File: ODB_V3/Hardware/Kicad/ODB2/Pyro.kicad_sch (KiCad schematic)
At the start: 51 parts, among them J6 Screw_Terminal_01x08, Q2 MMBT3904, Q3 SI7617DN-T1-GE3, U10 SI5442DU-T1-GE3, U11 SI5442DU-T1-GE3, U12 SI5442DU-T1-GE3, U13 SI5442DU-T1-GE3, U6 LM339

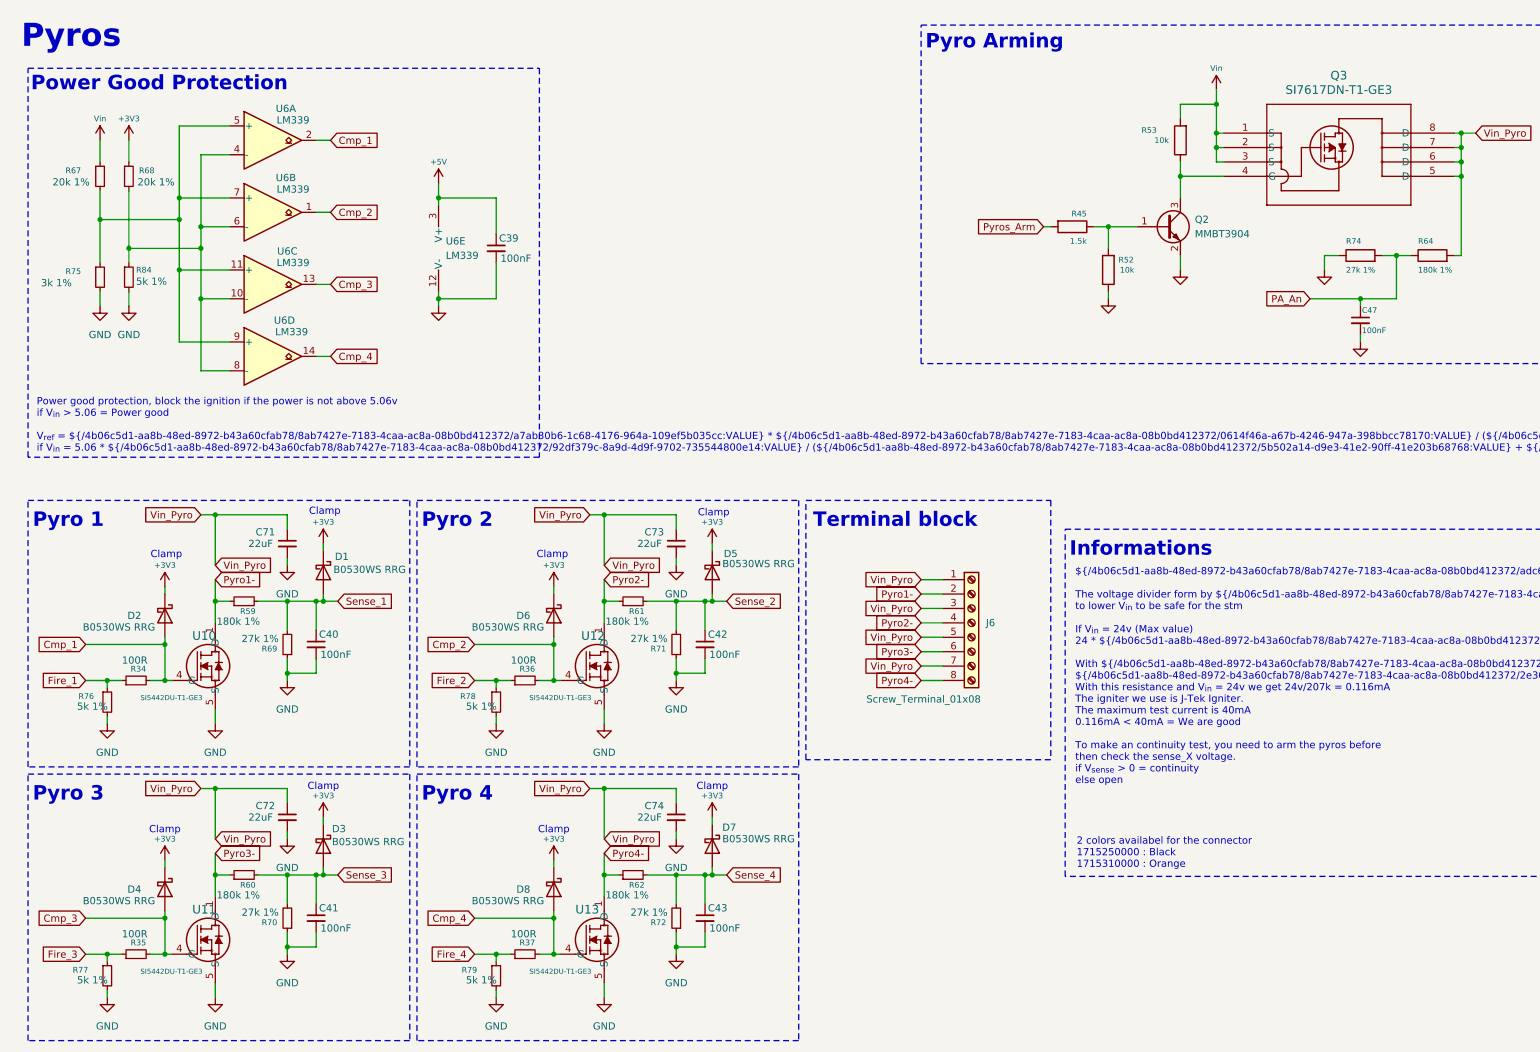
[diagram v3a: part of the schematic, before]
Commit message: wip : début refdes sur silkscreen
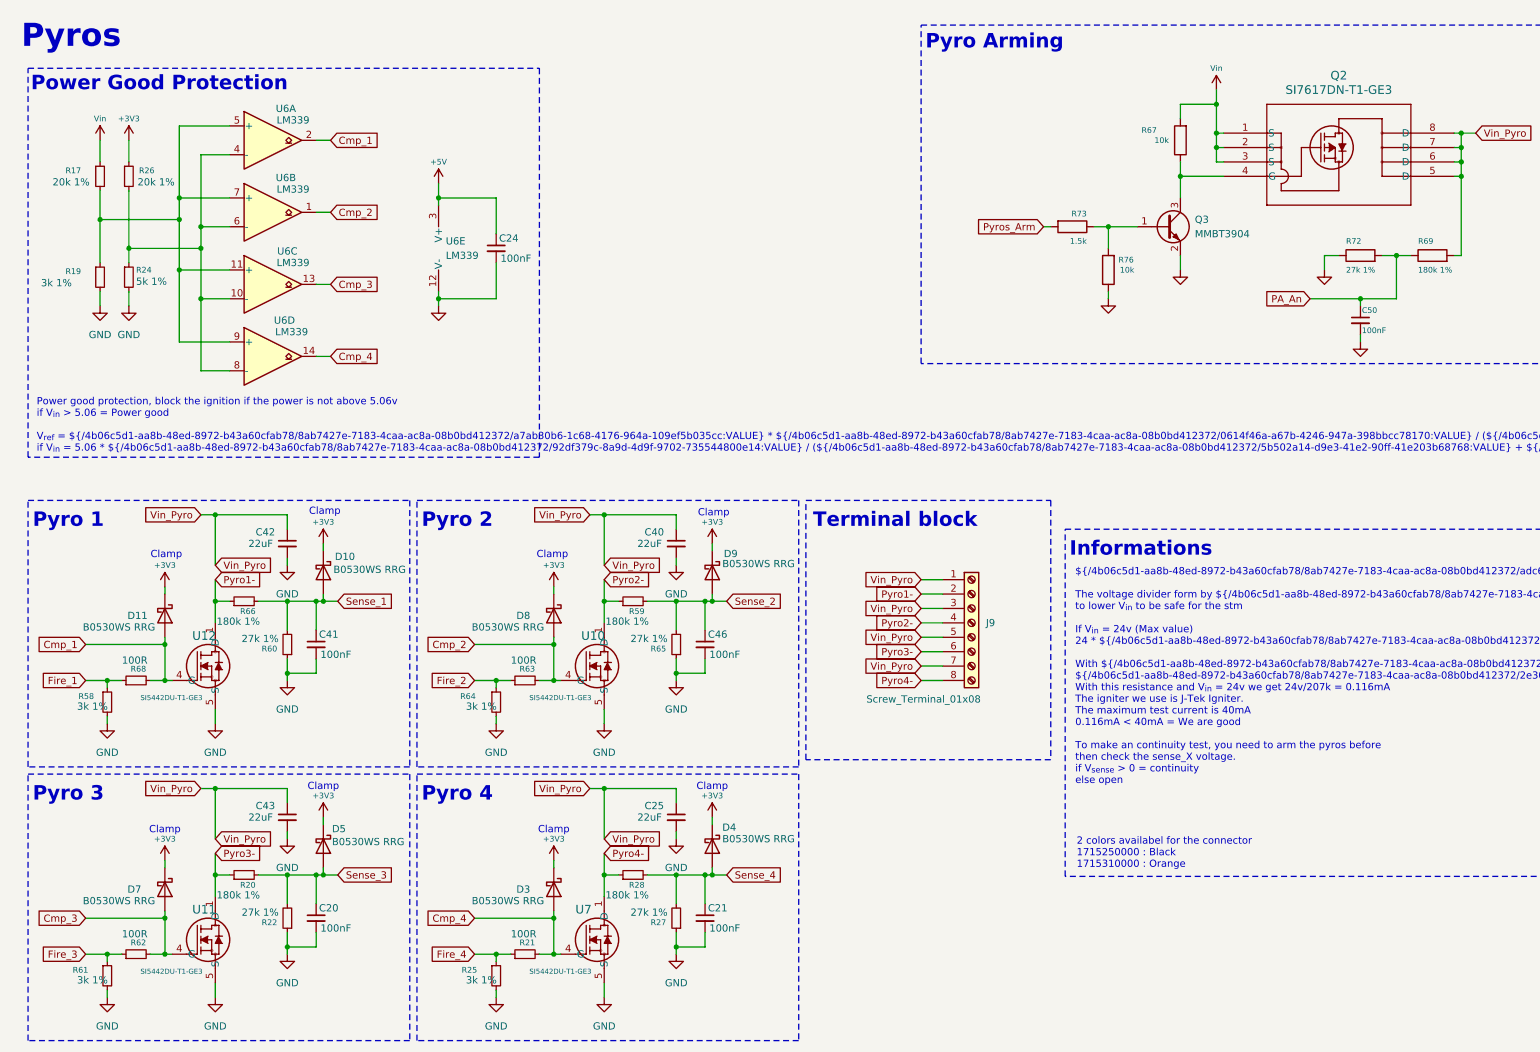
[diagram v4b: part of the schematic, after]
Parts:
- R25: renamed from R79; value 5k 1% -> 3k 1%
- R58: renamed from R76; value 5k 1% -> 3k 1%
- R61: renamed from R77; value 5k 1% -> 3k 1%
- R64: renamed from R78; value 5k 1% -> 3k 1%
- renumbered C41 to C20, C43 to C21, C39 to C24, C74 to C25, C73 to C40, C40 to C41, C71 to C42, C72 to C43, C42 to C46, C47 to C50, D1 to D10, D2 to D11, D8 to D3, D7 to D4, D3 to D5, D4 to D7, D6 to D8, D5 to D9, J6 to J9, Q3 to Q2, Q2 to Q3, R67 to R17, R75 to R19, R60 to R20, R37 to R21, R70 to R22, R84 to R24, R68 to R26, R72 to R27, R62 to R28, R61 to R59, R69 to R60, R35 to R62, R36 to R63, R71 to R65, R59 to R66, R53 to R67, R34 to R68, R64 to R69, R74 to R72, R45 to R73, R52 to R76, U12 to U10, U10 to U12, U13 to U7

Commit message: wip : fill all components in BOM
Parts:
- C20, C21, C24, C41, C46, C50: DigiKey_Part_Number (none) -> 311-3342-1-ND
- C25, C40, C42, C43: value 22uF -> 10uF; DigiKey_Part_Number (none) -> 490-13248-1-ND
- R17, R26: DigiKey_Part_Number (none) -> P20KDBCT-ND
- R19, R25, R58, R61, R64: DigiKey_Part_Number (none) -> RG16P3.0KBCT-ND
- R20, R28, R59, R66, R69: DigiKey_Part_Number (none) -> P180KDBCT-ND
- R21, R62, R63, R68: DigiKey_Part_Number (none) -> 764-1252-1-ND
- R22, R27, R60, R65, R72: DigiKey_Part_Number (none) -> RG16P27.0KBCT-ND
- R24: DigiKey_Part_Number (none) -> 13-RT0603BRE075KLCT-ND
- R67, R76: DigiKey_Part_Number (none) -> 311-10.0KHRCT-ND
- R73: DigiKey_Part_Number (none) -> 408-1766-1-ND

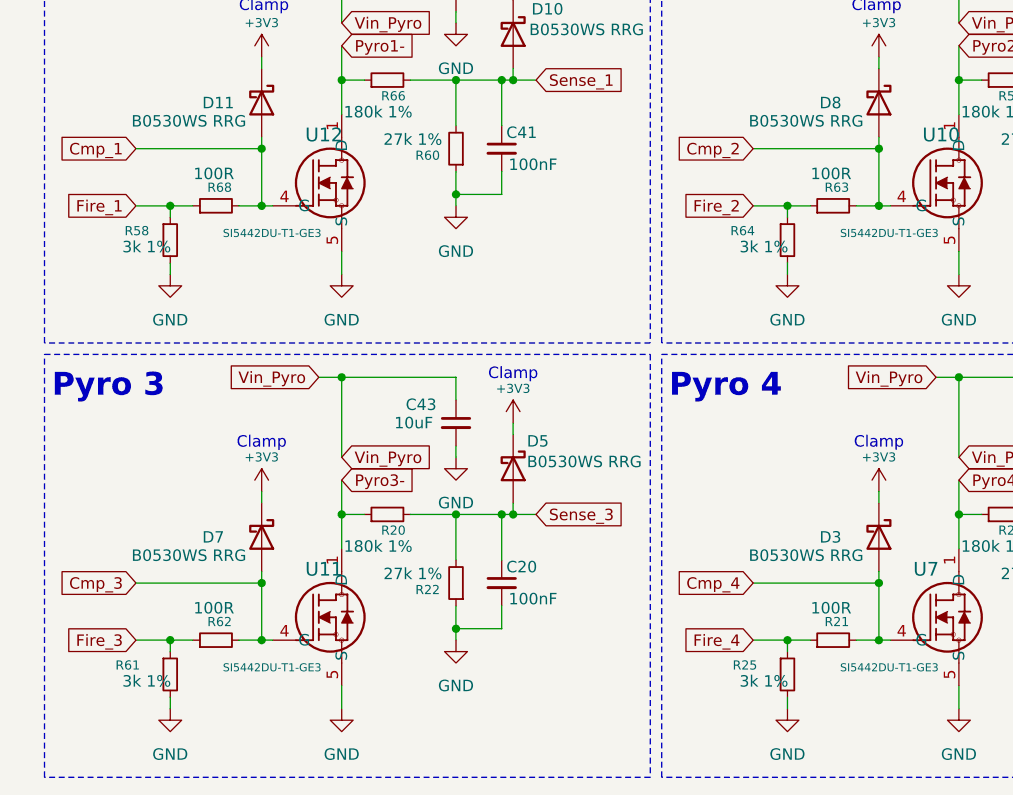
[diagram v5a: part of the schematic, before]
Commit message: wip : done filling BOM, fix silkscreen, fix NRST hardware
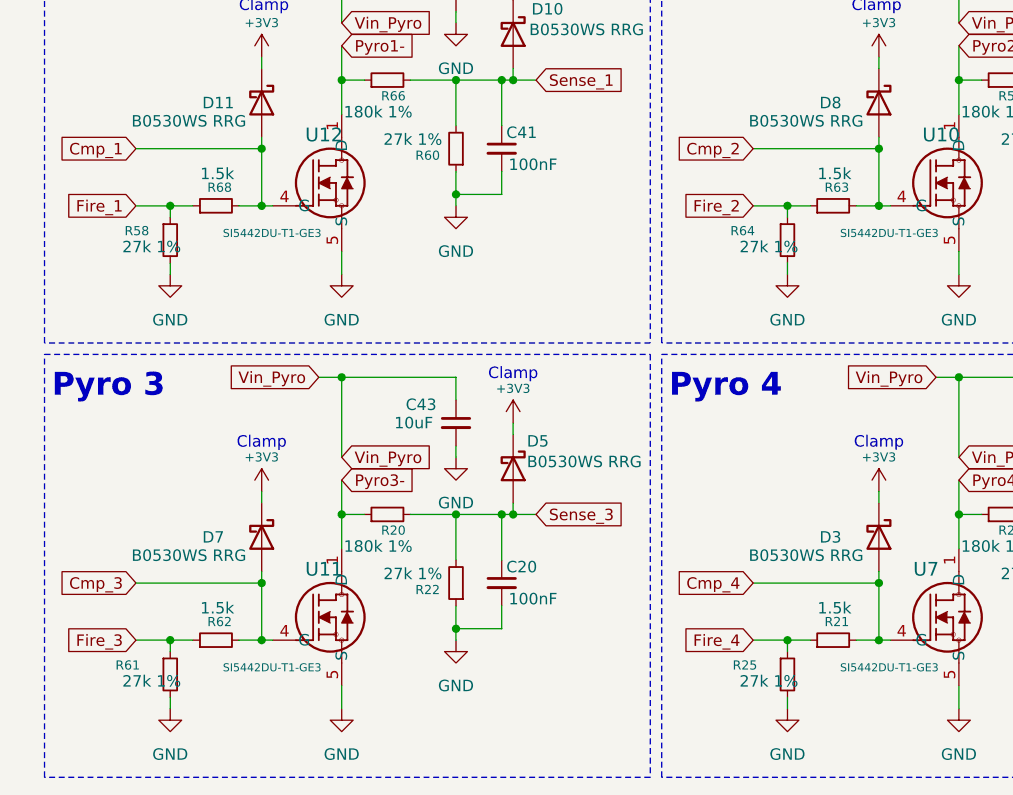
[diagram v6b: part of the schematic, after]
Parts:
- R21, R62, R63, R68: value 100R -> 1.5k; DigiKey_Part_Number 764-1252-1-ND -> 408-1766-1-ND
- R25, R58, R61, R64: value 3k 1% -> 27k 1%; DigiKey_Part_Number RG16P3.0KBCT-ND -> RG16P27.0KBCT-ND
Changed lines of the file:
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@@
 			)
 		)
-		(property "Value" "3k 1%"
+		(property "Value" "27k 1%"
 			(at 23.876 182.372 0)
 			(effects
@@
 			)
 		)
-		(property "Datasheet" "https://www.digikey.ca/en/products/detail/susumu/RG1608P-302-B-T5/1240549"
+		(property "Datasheet" "https://www.digikey.ca/en/products/detail/susumu/RG1608P-273-B-T5/1240540"
 			(at 29.21 181.61 0)
 			(effects
@@
 			)
 		)
-		(property "DigiKey_Part_Number" "RG16P3.0KBCT-ND"
+		(property "DigiKey_Part_Number" "RG16P27.0KBCT-ND"
 			(at 29.21 181.61 0)
 			(effects
@@
 			)
 		)
-		(property "Value" "100R"
+		(property "Value" "1.5k"
 			(at 104.902 174.244 90)
 			(effects
@@
 			)
 		)
-		(property "Datasheet" "https://www.digikey.ca/en/products/detail/vishay-dale-thin-film/PCAN0603E1000BST5/6003299"
+		(property "Datasheet" "https://www.digikey.ca/en/products/detail/susumu/URG1608L-152-L-T05/4552646"
 			(at 102.87 177.8 0)
 			(effects
@@
 			)
 		)
-		(property "DigiKey_Part_Number" "764-1252-1-ND"
+		(property "DigiKey_Part_Number" "408-1766-1-ND"
 			(at 102.87 177.8 90)
 			(effects
@@
 			)
 		)
-		(property "Value" "100R"
+		(property "Value" "1.5k"
 			(at 36.322 174.244 90)
 			(effects
@@
 			)
 		)
-		(property "Datasheet" "https://www.digikey.ca/en/products/detail/vishay-dale-thin-film/PCAN0603E1000BST5/6003299"
+		(property "Datasheet" "https://www.digikey.ca/en/products/detail/susumu/URG1608L-152-L-T05/4552646"
 			(at 34.29 177.8 0)
 			(effects
@@
 			)
 		)
-		(property "DigiKey_Part_Number" "764-1252-1-ND"
+		(property "DigiKey_Part_Number" "408-1766-1-ND"
 			(at 34.29 177.8 90)
 			(effects
@@
 			)
 		)
-		(property "Value" "100R"
+		(property "Value" "1.5k"
 			(at 104.902 125.984 90)
 			(effects
@@
 			)
 		)
-		(property "Datasheet" "https://www.digikey.ca/en/products/detail/vishay-dale-thin-film/PCAN0603E1000BST5/6003299"
+		(property "Datasheet" "https://www.digikey.ca/en/products/detail/susumu/URG1608L-152-L-T05/4552646"
 			(at 102.87 129.54 0)
 			(effects
@@
 			)
 		)
-		(property "DigiKey_Part_Number" "764-1252-1-ND"
+		(property "DigiKey_Part_Number" "408-1766-1-ND"
 			(at 102.87 129.54 90)
 			(effects
@@
 			)
 		)
-		(property "Value" "3k 1%"
+		(property "Value" "27k 1%"
 			(at 92.456 182.372 0)
 			(effects
@@
 			)
 		)
-		(property "Datasheet" "https://www.digikey.ca/en/products/detail/susumu/RG1608P-302-B-T5/1240549"
+		(property "Datasheet" "https://www.digikey.ca/en/products/detail/susumu/RG1608P-273-B-T5/1240540"
 			(at 97.79 181.61 0)
 			(effects
@@
 			)
 		)
-		(property "DigiKey_Part_Number" "RG16P3.0KBCT-ND"
+		(property "DigiKey_Part_Number" "RG16P27.0KBCT-ND"
 			(at 97.79 181.61 0)
 			(effects
@@
 			)
 		)
-		(property "Value" "3k 1%"
+		(property "Value" "27k 1%"
 			(at 23.876 134.112 0)
 			(effects
@@
 			)
 		)
-		(property "Datasheet" "https://www.digikey.ca/en/products/detail/susumu/RG1608P-302-B-T5/1240549"
+		(property "Datasheet" "https://www.digikey.ca/en/products/detail/susumu/RG1608P-273-B-T5/1240540"
 			(at 29.21 133.35 0)
 			(effects
@@
 			)
 		)
-		(property "DigiKey_Part_Number" "RG16P3.0KBCT-ND"
+		(property "DigiKey_Part_Number" "RG16P27.0KBCT-ND"
 			(at 29.21 133.35 0)
 			(effects
@@
 			)
 		)
-		(property "Value" "3k 1%"
+		(property "Value" "27k 1%"
 			(at 92.456 134.112 0)
 			(effects
@@
 			)
 		)
-		(property "Datasheet" "https://www.digikey.ca/en/products/detail/susumu/RG1608P-302-B-T5/1240549"
+		(property "Datasheet" "https://www.digikey.ca/en/products/detail/susumu/RG1608P-273-B-T5/1240540"
 			(at 97.79 133.35 0)
 			(effects
@@
 			)
 		)
-		(property "DigiKey_Part_Number" "RG16P3.0KBCT-ND"
+		(property "DigiKey_Part_Number" "RG16P27.0KBCT-ND"
 			(at 97.79 133.35 0)
 			(effects
@@
 			)
 		)
-		(property "Value" "100R"
+		(property "Value" "1.5k"
 			(at 36.322 125.984 90)
 			(effects
@@
 			)
 		)
-		(property "Datasheet" "https://www.digikey.ca/en/products/detail/vishay-dale-thin-film/PCAN0603E1000BST5/6003299"
+		(property "Datasheet" "https://www.digikey.ca/en/products/detail/susumu/URG1608L-152-L-T05/4552646"
 			(at 34.29 129.54 0)
 			(effects
@@
 			)
 		)
-		(property "DigiKey_Part_Number" "764-1252-1-ND"
+		(property "DigiKey_Part_Number" "408-1766-1-ND"
 			(at 34.29 129.54 90)
 			(effects

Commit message: wip : add MPN and fix footprints
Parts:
- C20, C21, C24, C41, C46, C50: Manufacturer_Part_Number (none) -> CC0402KRX5R9BB104
- C25, C40, C42, C43: Manufacturer_Part_Number (none) -> GRM188R6YA106MA73D
- D10, D11, D3, D4, D5, D7, D8, D9: value B0530WS RRG -> NSR0620P2T5G; DigiKey_Part_Number B0530WSRRGCT-ND -> NSR0620P2T5GOSCT-ND; Manufacturer_Part_Number (none) -> NSR0620P2T5G
- J9: Manufacturer_Part_Number (none) -> 1725711
- Q2: Manufacturer_Part_Number (none) -> SI7617DN-T1-GE3
- Q3: Manufacturer_Part_Number (none) -> MMBT3904LT1G
- R17, R26: Manufacturer_Part_Number (none) -> ERA-3AEB203V
- R19: value 3k 1% -> 5k 1%; DigiKey_Part_Number RG16P3.0KBCT-ND -> 13-RT0603BRE075KLCT-ND; Manufacturer_Part_Number (none) -> RT0603BRE075KL
- R20, R28, R59, R66, R69: Manufacturer_Part_Number (none) -> ERA-3AEB184V
- R21, R62, R63, R68, R73: Manufacturer_Part_Number (none) -> URG1608L-152-L-T05
- R22, R25, R27, R58, R60, R61, R64, R65, R72: Manufacturer_Part_Number (none) -> RG1608P-273-B-T5
- R24: Manufacturer_Part_Number (none) -> RT0603BRE075KL
- R67, R76: Manufacturer_Part_Number (none) -> RC0603FR-0710KL
- U10, U11, U12, U7: Manufacturer_Part_Number (none) -> SI5442DU-T1-GE3
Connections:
- net +3V3: no longer R26.1
- net +5V: now also R26.1
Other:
- note added: "Power good protection, block the ignition if the power is not above 5.00v if V_{in} > 5.0 = Power good V_{ref} = 5V * ${/4b06c5d1-aa8b-48ed-8972-b43a60cfab78/8ab7427e-7183-4caa-ac8a-08b0bd412372/0614f46a-a67b-4246-947a-398bbcc78170:VALUE} / (${/4b06c5d1-aa8b-48ed-8972-b43a60cfab78/8ab7427e-7183-4caa-ac8a-08b0bd412372/0f2812a9-637d-4404-af99-83782ba39a65:VALUE} + ${/4b06c5d1-aa8b-48ed-8972-b43a60c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"
- note removed: "Power good protection, block the ignition if the power is not above 5.06v if V_{in} > 5.06 = Power good V_{ref} = ${/4b06c5d1-aa8b-48ed-8972-b43a60cfab78/8ab7427e-7183-4caa-ac8a-08b0bd412372/a7ab30b6-1c68-4176-964a-109ef5b035cc:VALUE} * ${/4b06c5d1-aa8b-48ed-8972-b43a60cfab78/8ab7427e-7183-4caa-ac8a-08b0bd412372/0614f46a-a67b-4246-947a-398bbcc78170:VALUE} / (${/4b06c5d1-aa8b-48ed-8972-b43a60cfab7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"
